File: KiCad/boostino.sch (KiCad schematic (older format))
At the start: 18 parts, among them J1 Conn_01x14_Female, J2 Conn_01x04_Male, Q1 2N3904, U1 Teensy3.6, U2 MC33660

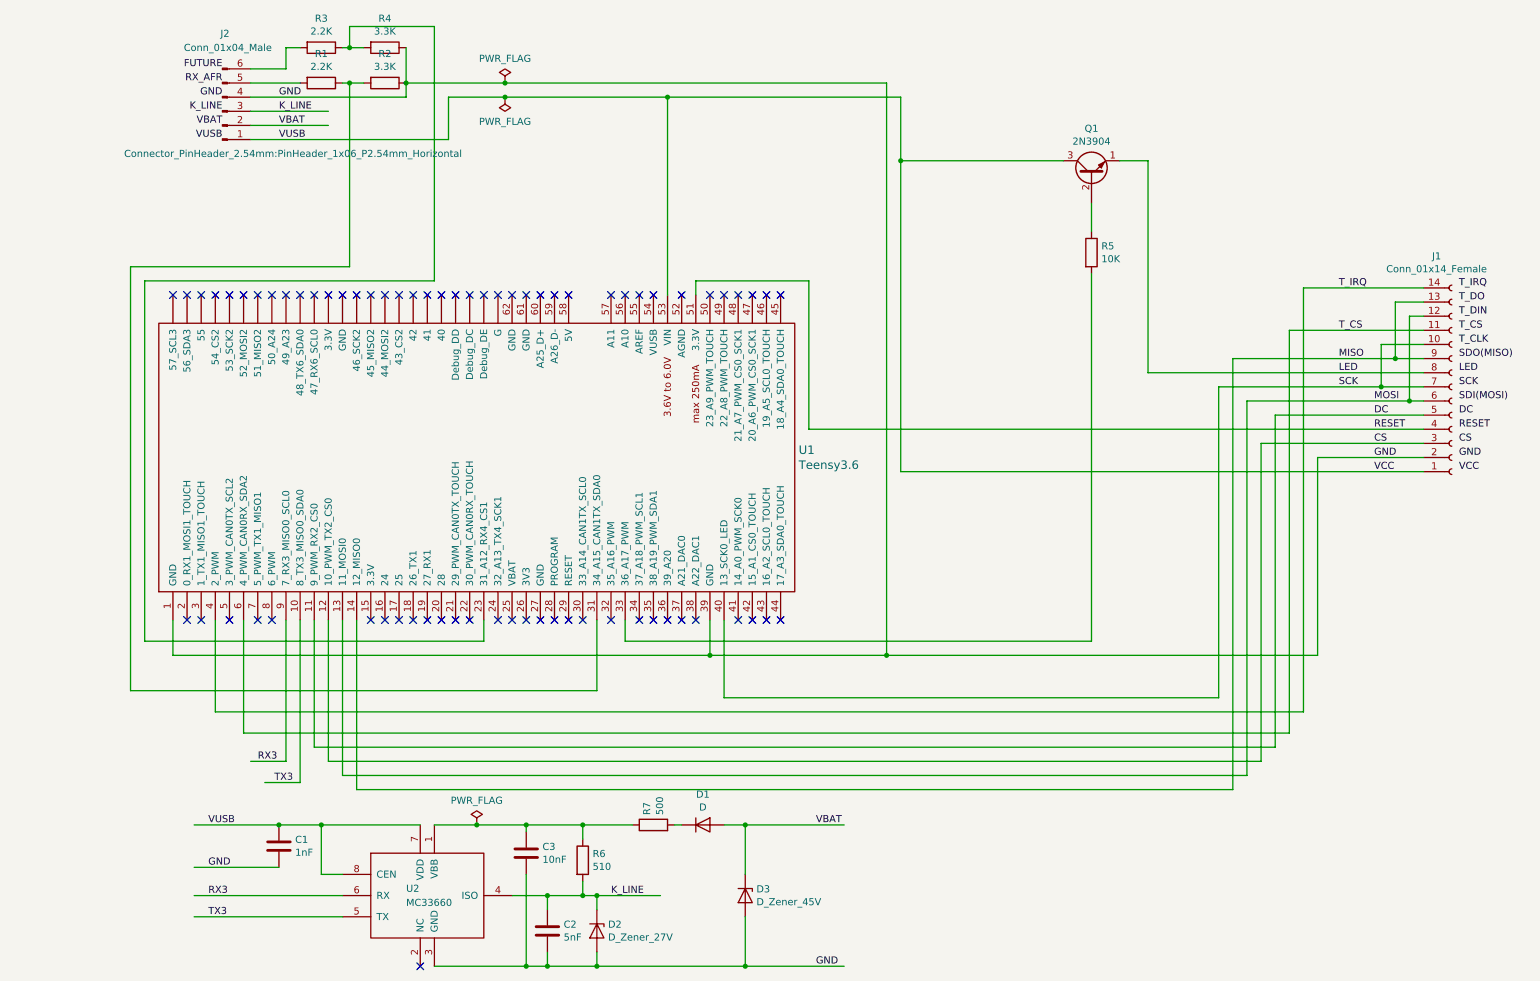
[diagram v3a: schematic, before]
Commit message: Update component values.
Alternate values in brackets where applicable.
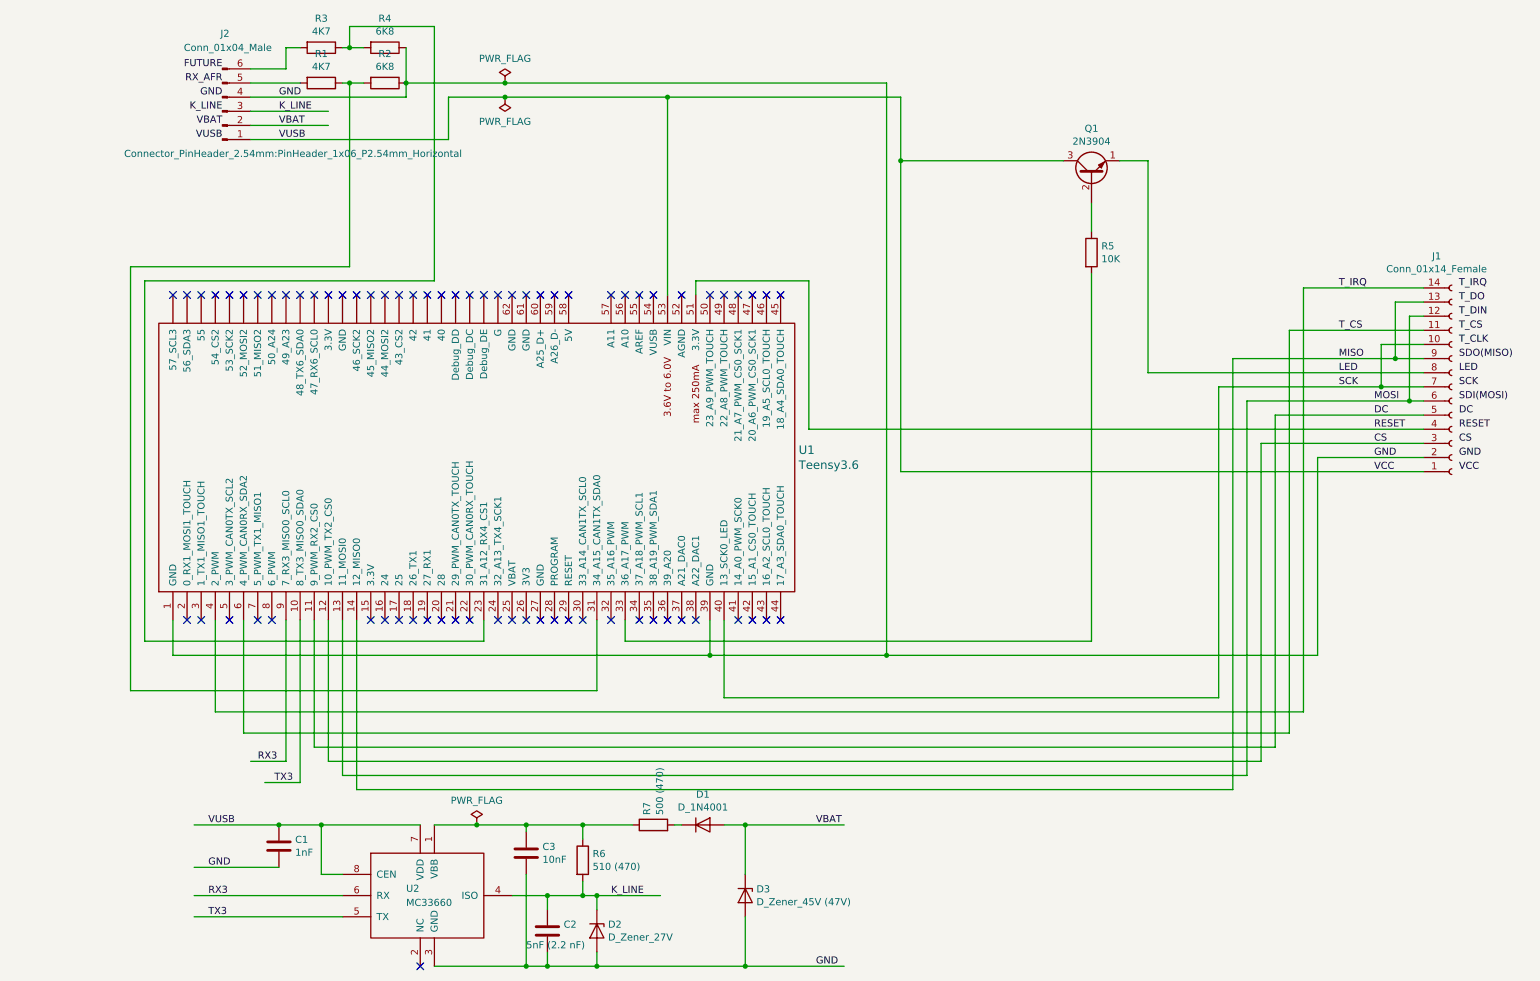
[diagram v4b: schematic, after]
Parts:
- C2: value 5nF -> 5nF (2.2 nF)
- D1: value D -> D_1N4001
- D3: value D_Zener_45V -> D_Zener_45V (47V)
- R1, R3: value 2.2K -> 4K7
- R2, R4: value 3.3K -> 6K8
- R6: value 510 -> 510 (470)
- R7: value 500 -> 500 (470)
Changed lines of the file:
@@
 P 2000 1300
 F 0 "R1" V 1793 1300 50  0000 C CNN
-F 1 "2.2K" V 1884 1300 50  0000 C CNN
+F 1 "4K7" V 1884 1300 50  0000 C CNN
 F 2 "Resistor_SMD:R_0805_2012Metric_Pad1.15x1.40mm_HandSolder" V 1930 1300 50  0001 C CNN
 F 3 "~" H 2000 1300 50  0001 C CNN
@@
 P 2000 1050
 F 0 "R3" V 1793 1050 50  0000 C CNN
-F 1 "2.2K" V 1884 1050 50  0000 C CNN
+F 1 "4K7" V 1884 1050 50  0000 C CNN
 F 2 "Resistor_SMD:R_0805_2012Metric_Pad1.15x1.40mm_HandSolder" V 1930 1050 50  0001 C CNN
 F 3 "~" H 2000 1050 50  0001 C CNN
@@
 P 2450 1050
 F 0 "R4" V 2243 1050 50  0000 C CNN
-F 1 "3.3K" V 2334 1050 50  0000 C CNN
+F 1 "6K8" V 2334 1050 50  0000 C CNN
 F 2 "Resistor_SMD:R_0805_2012Metric_Pad1.15x1.40mm_HandSolder" V 2380 1050 50  0001 C CNN
 F 3 "~" H 2450 1050 50  0001 C CNN
@@
 P 2450 1300
 F 0 "R2" V 2243 1300 50  0000 C CNN
-F 1 "3.3K" V 2334 1300 50  0000 C CNN
+F 1 "6K8" V 2334 1300 50  0000 C CNN
 F 2 "Resistor_SMD:R_0805_2012Metric_Pad1.15x1.40mm_HandSolder" V 2380 1300 50  0001 C CNN
 F 3 "~" H 2450 1300 50  0001 C CNN
@@
 P 3850 6800
 F 0 "R6" H 3920 6846 50  0000 L CNN
-F 1 "510" H 3920 6755 50  0000 L CNN
+F 1 "510 (470)" H 3920 6755 50  0000 L CNN
 F 2 "Resistor_SMD:R_0805_2012Metric_Pad1.15x1.40mm_HandSolder" V 3780 6800 50  0001 C CNN
 F 3 "~" H 3850 6800 50  0001 C CNN
@@
 P 4350 6550
 F 0 "R7" H 4420 6596 50  0000 L CNN
-F 1 "500" H 4420 6505 50  0000 L CNN
+F 1 "500 (470)" H 4420 6505 50  0000 L CNN
 F 2 "Resistor_SMD:R_0805_2012Metric_Pad1.15x1.40mm_HandSolder" V 4280 6550 50  0001 C CNN
 F 3 "~" H 4350 6550 50  0001 C CNN
@@
 P 5000 7050
 F 0 "D3" V 4954 7129 50  0000 L CNN
-F 1 "D_Zener_45V" V 5045 7129 50  0000 L CNN
+F 1 "D_Zener_45V (47V)" V 5045 7129 50  0000 L CNN
 F 2 "Diode_SMD:D_MiniMELF_Handsoldering" H 5000 7050 50  0001 C CNN
 F 3 "~" H 5000 7050 50  0001 C CNN
@@
 P 3600 7300
 F 0 "C2" H 3485 7254 50  0000 R CNN
-F 1 "5nF" H 3485 7345 50  0000 R CNN
+F 1 "5nF (2.2 nF)" H 3750 7400 50  0000 R CNN
 F 2 "Capacitor_SMD:C_1206_3216Metric_Pad1.42x1.75mm_HandSolder" H 3638 7150 50  0001 C CNN
 F 3 "~" H 3600 7300 50  0001 C CNN
@@
 	1700 6550 2000 6550
 NoConn ~ 1650 5100
-$Comp
-L Device:D D1
-U 1 1 5F78823F
-P 4700 6550
-F 0 "D1" H 4700 6766 50  0000 C CNN
-F 1 "D" H 4700 6675 50  0000 C CNN
-F 2 "Diode_THT:D_A-405_P10.16mm_Horizontal" H 4700 6550 50  0001 C CNN
-F 3 "~" H 4700 6550 50  0001 C CNN
-	1    4700 6550
-	1    0    0    -1
-$EndComp
 Text Label 1550 6100 0    50   ~ 0
 RX3
@@
 NoConn ~ 2650 5100
 NoConn ~ 2750 5100
+$Comp
+L Device:D D1
+U 1 1 5F78823F
+P 4700 6550
+F 0 "D1" H 4700 6766 50  0000 C CNN
+F 1 "D_1N4001" H 4700 6675 50  0000 C CNN
+F 2 "Diode_THT:D_A-405_P10.16mm_Horizontal" H 4700 6550 50  0001 C CNN
+F 3 "~" H 4700 6550 50  0001 C CNN
+	1    4700 6550
+	1    0    0    -1
+$EndComp
 $EndSCHEMATC
